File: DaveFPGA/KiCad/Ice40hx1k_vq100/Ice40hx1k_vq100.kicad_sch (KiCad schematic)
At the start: 153 parts, among them J1 +5V, J10 VGA, J2 +3v3, J3 USB_B_Micro, J4 VGA, J5 SWD, U1 LD1117S33TR_SOT223, U10 74CBTD3861, U11 LSF0108PW, U12 74CBTD3861, U2 MIC5504-1.2YM5, U3 iCE40HX4K-TQ144, U4 TLV74311PDBVR, U5 RP2354A-QFN60, U6 LSF0108PW, U7 74CBTD3861, U8 74CBTD3861, U9 LSF0108PW, Y1 12MHz

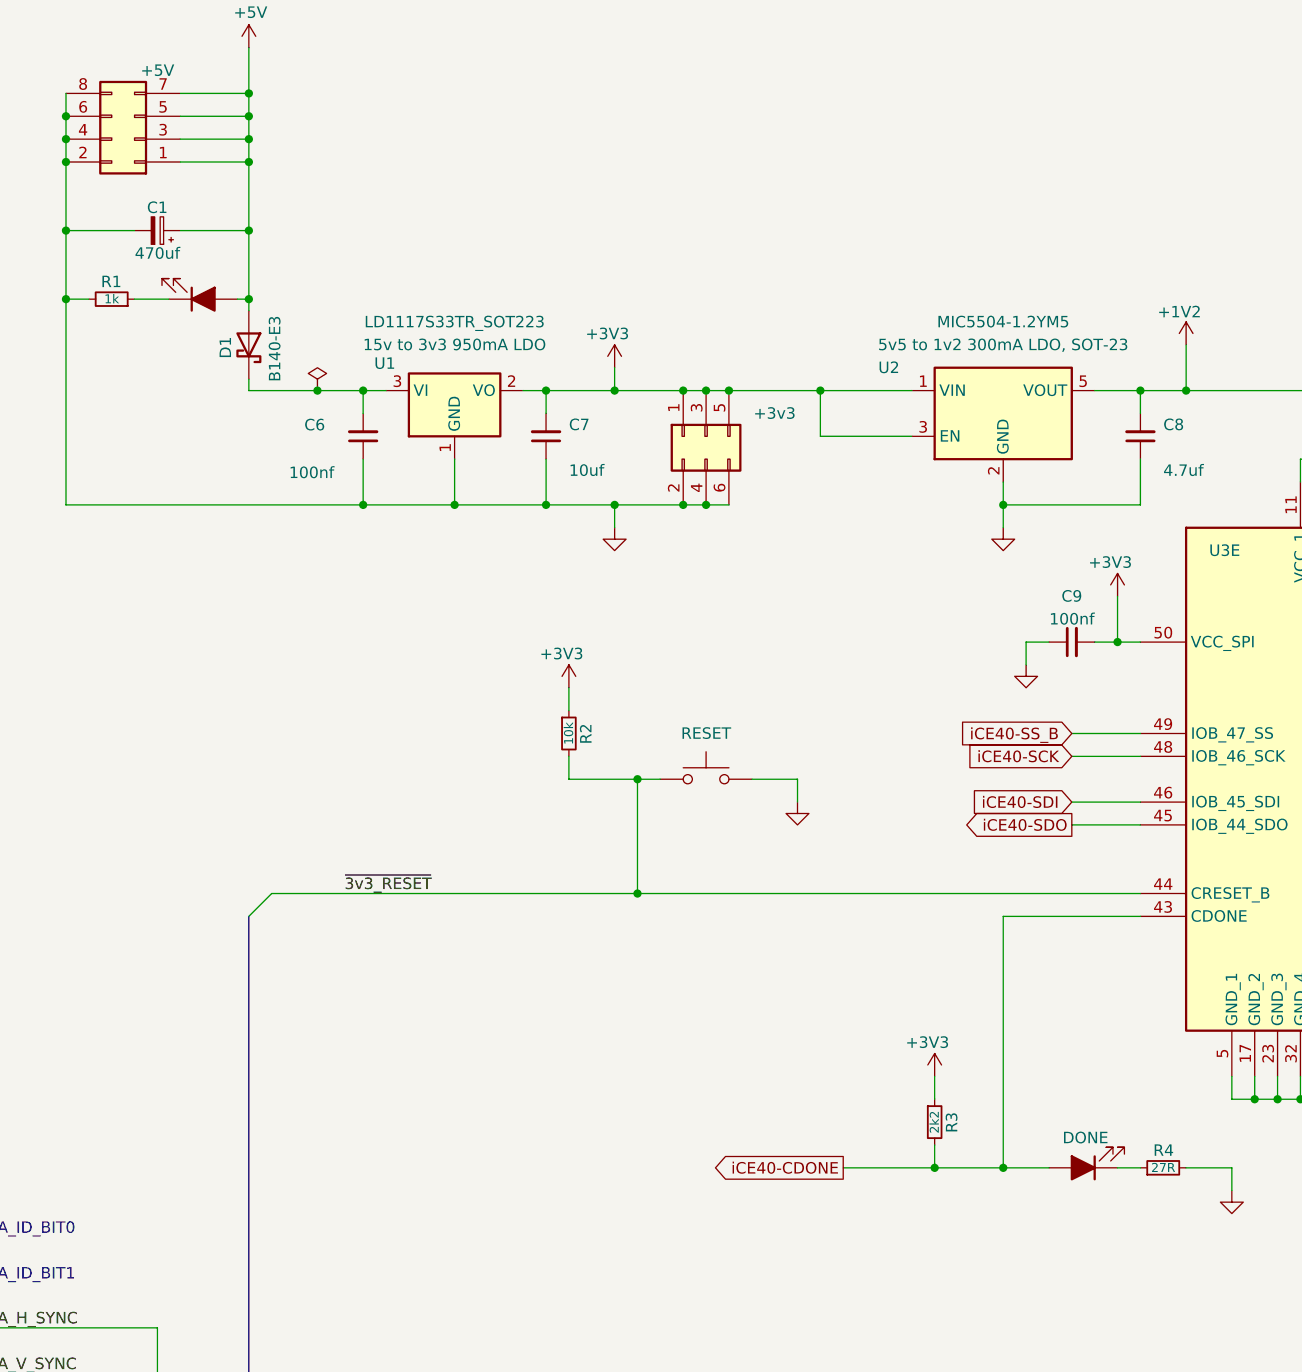
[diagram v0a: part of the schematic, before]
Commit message: - Updated to kicad 10.0.6
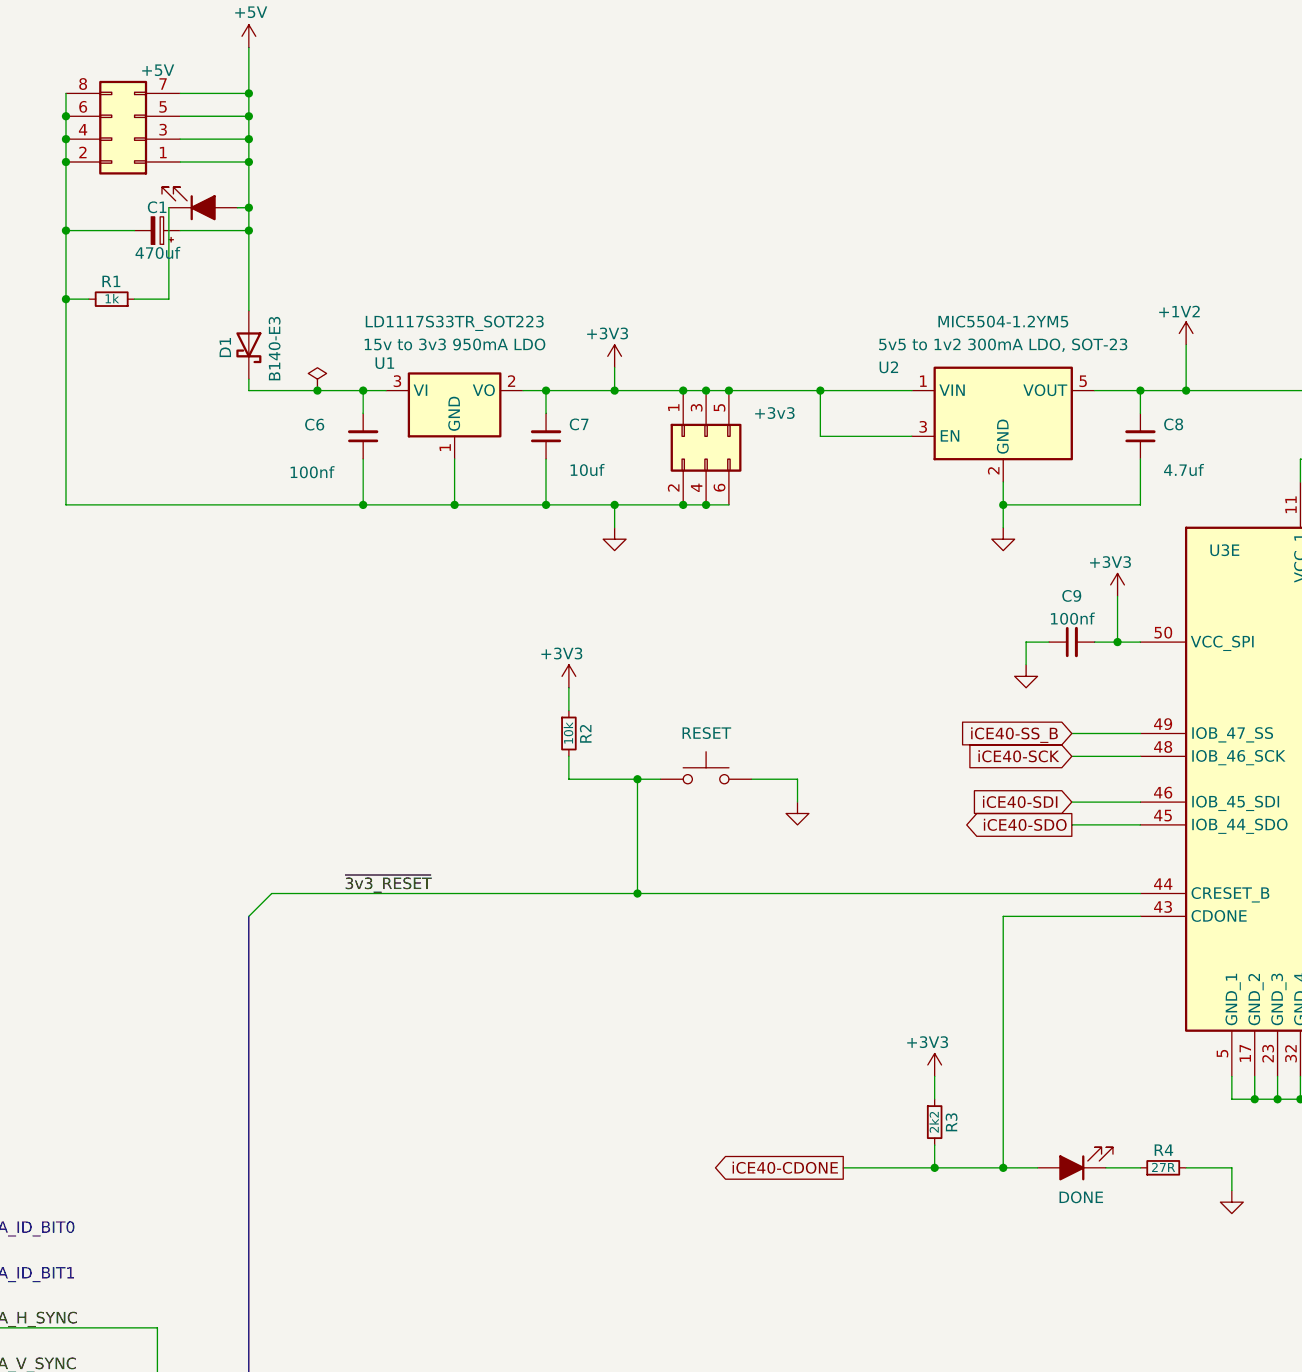
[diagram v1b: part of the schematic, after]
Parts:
- CDone1: symbol Dave:LED -> Device:LED_Filled
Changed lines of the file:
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@@
 	)
 	(junction
-		(at 345.44 76.2)
+		(at 345.44 66.04)
 		(diameter 0)
 		(color 0 0 0 0)
@@
 	(wire
 		(pts
+			(xy 336.55 76.2) (xy 332.74 76.2)
+		)
+		(stroke
+			(width 0)
+			(type default)
+		)
+	)
+	(wire
+		(pts
 			(xy 406.4 299.72) (xy 406.4 314.96)
 		)
@@
 	(wire
 		(pts
-			(xy 345.44 68.58) (xy 345.44 76.2)
-		)
-		(stroke
-			(width 0)
-			(type default)
-		)
-	)
-	(wire
-		(pts
 			(xy 312.42 195.58) (xy 340.36 195.58)
 		)
@@
 	(wire
 		(pts
-			(xy 345.44 60.96) (xy 345.44 68.58)
+			(xy 345.44 60.96) (xy 345.44 77.47)
 		)
 		(stroke
@@
 	(wire
 		(pts
+			(xy 336.55 66.04) (xy 336.55 76.2)
+		)
+		(stroke
+			(width 0)
+			(type default)
+		)
+	)
+	(wire
+		(pts
 			(xy 759.46 482.6) (xy 746.76 482.6)
 		)
@@
 	(wire
 		(pts
-			(xy 345.44 76.2) (xy 345.44 77.47)
-		)
-		(stroke
-			(width 0)
-			(type default)
-		)
-	)
-	(wire
-		(pts
 			(xy 66.04 233.68) (xy 101.6 233.68)
 		)
@@
 	(wire
 		(pts
-			(xy 336.55 76.2) (xy 332.74 76.2)
-		)
-		(stroke
-			(width 0)
-			(type default)
-		)
-	)
-	(wire
-		(pts
 			(xy 759.46 419.1) (xy 746.76 419.1)
 		)
@@
 	(wire
 		(pts
-			(xy 344.17 76.2) (xy 345.44 76.2)
+			(xy 344.17 66.04) (xy 345.44 66.04)
 		)
 		(stroke
@@
 	(wire
 		(pts
+			(xy 440.69 172.72) (xy 444.5 172.72)
+		)
+		(stroke
+			(width 0)
+			(type default)
+		)
+	)
+	(wire
+		(pts
 			(xy 264.16 429.26) (xy 302.26 429.26)
 		)
@@
 	(wire
 		(pts
-			(xy 429.26 172.72) (xy 434.34 172.72)
+			(xy 429.26 172.72) (xy 433.07 172.72)
 		)
 		(stroke
@@
 	(wire
 		(pts
-			(xy 441.96 172.72) (xy 444.5 172.72)
-		)
-		(stroke
-			(width 0)
-			(type default)
-		)
-	)
-	(wire
-		(pts
 			(xy 195.58 149.86) (xy 185.42 149.86)
 		)
@@
 	)
 	(symbol
-		(lib_id "Dave:LED")
-		(at 439.42 172.72 0)
+		(lib_id "Device:LED_Filled")
+		(at 436.88 172.72 180)
 		(unit 1)
 		(body_style 1)
@@
 		(dnp no)
 		(property "Reference" "CDone1"
-			(at 443.23 170.18 0)
+			(at 433.07 175.26 0)
 			(hide yes)
 			(show_name no)
@@
 		)
 		(property "Value" "DONE"
-			(at 440.9556 169.3969 0)
+			(at 435.3444 176.0431 0)
 			(show_name no)
 			(do_not_autoplace no)
@@
 		)
 		(property "Description" "Light emitting diode, filled shape"
-			(at 439.674 180.086 0)
+			(at 436.626 165.354 0)
 			(hide yes)
 			(show_name no)
@@
 		)
 		(property "Note" ""
-			(at 439.42 172.72 0)
+			(at 436.88 172.72 0)
 			(hide yes)
 			(show_name no)
@@
 		)
 		(property "Voltage" ""
-			(at 439.42 172.72 0)
+			(at 436.88 172.72 0)
 			(hide yes)
 			(show_name no)
@@
 		)
 		(property "class" ""
-			(at 439.42 172.72 0)
+			(at 436.88 172.72 0)
 			(hide yes)
 			(show_name no)
@@
 	(symbol
 		(lib_id "Device:LED_Filled")
-		(at 340.36 76.2 0)
+		(at 340.36 66.04 0)
 		(mirror x)
 		(unit 1)
@@
 		(dnp no)
 		(property "Reference" "Power1"
-			(at 339.09 78.74 0)
+			(at 339.09 68.58 0)
 			(hide yes)
 			(show_name no)
@@
 		)
 		(property "Value" "POWER"
-			(at 337.5026 72.39 90)
+			(at 337.5026 62.23 90)
 			(hide yes)
 			(show_name no)
@@
 		)
 		(property "Footprint" "LED_SMD:LED_0805_2012Metric"
-			(at 340.36 76.2 0)
+			(at 340.36 66.04 0)
 			(hide yes)
 			(show_name no)
@@
 		)
 		(property "Datasheet" ""
-			(at 340.36 76.2 0)
+			(at 340.36 66.04 0)
 			(hide yes)
 			(show_name no)
@@
 		)
 		(property "Description" "Light emitting diode, filled shape"
-			(at 340.36 76.2 0)
+			(at 340.36 66.04 0)
 			(hide yes)
 			(show_name no)
@@
 		)
 		(property "Note" ""
-			(at 340.36 76.2 0)
+			(at 340.36 66.04 0)
 			(hide yes)
 			(show_name no)
@@
 		)
 		(property "Voltage" ""
-			(at 340.36 76.2 0)
+			(at 340.36 66.04 0)
 			(hide yes)
 			(show_name no)
@@
 		)
 		(property "class" ""
-			(at 340.36 76.2 0)
+			(at 340.36 66.04 0)
 			(hide yes)
 			(show_name no)
@@
 		)
 		(property "Sim.Pins" "1=K 2=A"
-			(at 340.36 76.2 0)
+			(at 340.36 66.04 0)
 			(hide yes)
 			(show_name no)
@@
 		)
 		(property "Height" ""
-			(at 340.36 76.2 0)
+			(at 340.36 66.04 0)
 			(hide yes)
 			(show_name no)
@@
 		)
 		(property "Manufacturer_Name" ""
-			(at 340.36 76.2 0)
+			(at 340.36 66.04 0)
 			(hide yes)
 			(show_name no)
@@
 		)
 		(property "Manufacturer_Part_Number" ""
-			(at 340.36 76.2 0)
+			(at 340.36 66.04 0)
 			(hide yes)
 			(show_name no)
@@
 		)
 		(property "Mouser Part Number" ""
-			(at 340.36 76.2 0)
+			(at 340.36 66.04 0)
 			(hide yes)
 			(show_name no)
@@
 		)
 		(property "Mouser Price/Stock" ""
-			(at 340.36 76.2 0)
+			(at 340.36 66.04 0)
 			(hide yes)
 			(show_name no)

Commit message: - Created a new FPGA prototyping board based around the iCE40hx1k and the rp2354.
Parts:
- U3: value iCE40HX4K-TQ144 -> iCE40HX1K-VQ100
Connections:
- net ~{3v3_RESET}: no longer S1.1
- net at R22.2, U5.26 (RUN): now also S1.1
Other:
- moved on the sheet: C1, C25, C26, R1, R11, R12, R2, R21

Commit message: - Created design blocks for the RP2354 and iCE40hx1k_vq100
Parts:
- added C55: 100nf, Capacitor_SMD:C_0603_1608Metric, symbol Device:C_Small
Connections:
- net +3V3: now also C55.2
- net GND: now also C55.1
